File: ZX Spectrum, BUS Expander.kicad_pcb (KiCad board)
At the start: 2 copper layers, 90 x 87.4 mm, 13 parts, among them J1 Conn_02x28_Row_Letter_First, J2 Conn_02x28_Row_Letter_First

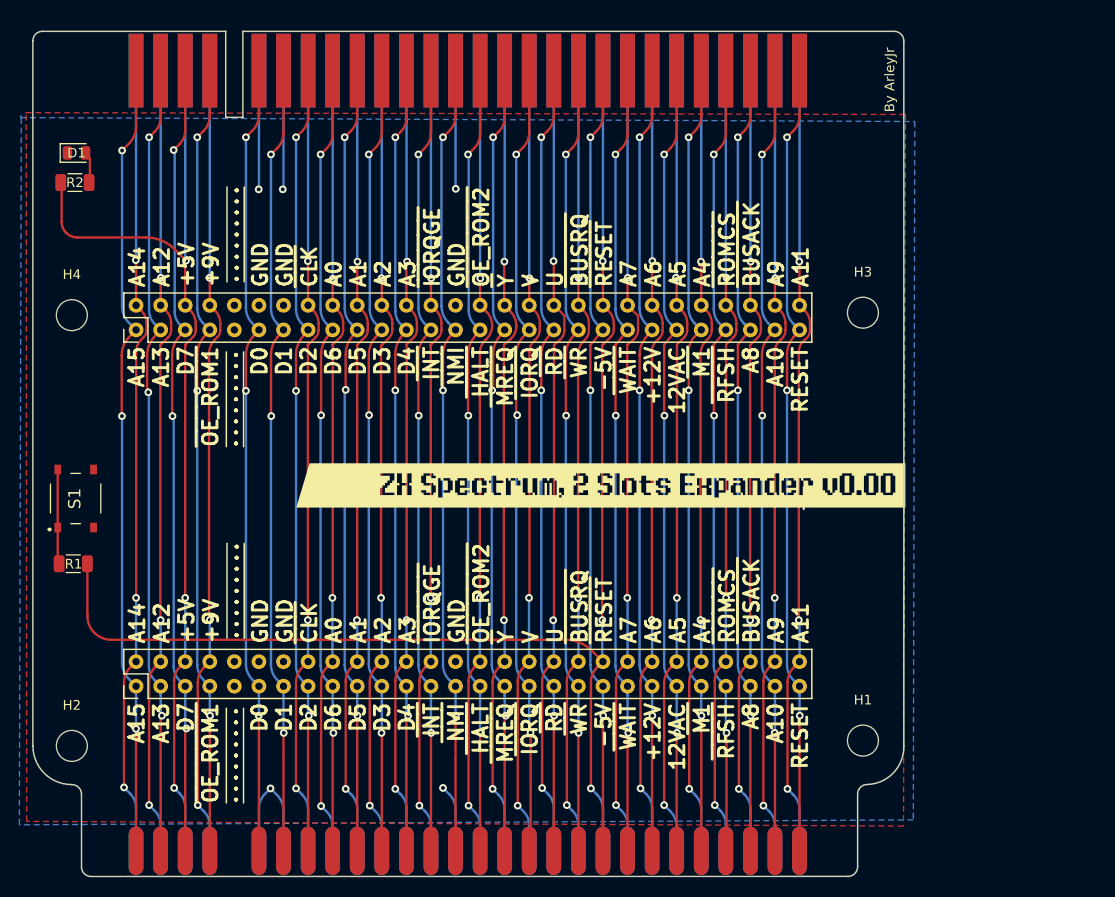
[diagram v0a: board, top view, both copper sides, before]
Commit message: Added Nemo BUS
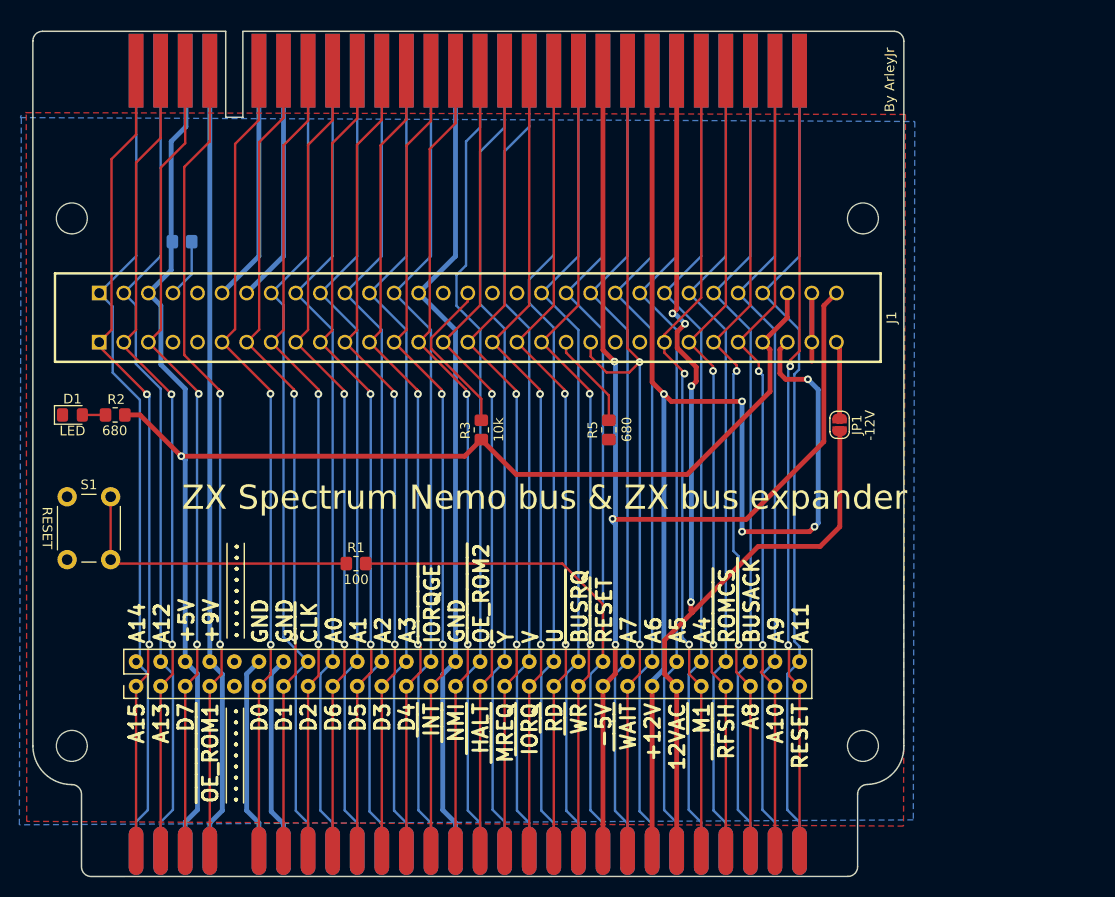
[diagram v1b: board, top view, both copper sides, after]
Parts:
- removed kibuzzard-65E37D50: G***, kibuzzard-65E37D50
- added JP1: -12V, Jumper:SolderJumper-2_P1.3mm_Open_RoundedPad1.0x1.5mm, F.Cu at (178.2, 92.4)
- added R3: 10k, Resistor_SMD:R_0805_2012Metric_Pad1.20x1.40mm_HandSolder, F.Cu at (141.2, 92.9)
- added R4: 10k, Resistor_SMD:R_0805_2012Metric_Pad1.20x1.40mm_HandSolder, B.Cu at (110.2, 73.4)
- added R5: 680, Resistor_SMD:R_0805_2012Metric_Pad1.20x1.40mm_HandSolder, F.Cu at (154.4, 92.9)
- D1: footprint LED_SMD:LED_0805_2012Metric -> LED_SMD:LED_0805_2012Metric_Pad1.15x1.40mm_HandSolder
- J1: value Conn_02x28_Row_Letter_First -> SL-62; footprint My Footprint Library, Sinclair:ZX Bus Socket -> zxbus:NemoBus-SL62-inverted
- R1: value 100R -> 100; footprint Resistor_SMD:R_1206_3216Metric -> Resistor_SMD:R_0805_2012Metric_Pad1.20x1.40mm_HandSolder
- R2: value 330R -> 680; footprint Resistor_SMD:R_1206_3216Metric -> Resistor_SMD:R_0805_2012Metric_Pad1.20x1.40mm_HandSolder
- S1: value PTS526_SM15_SMTR2_LFS -> RESET; footprint My Footprint Library:PTS526SM15SMTR2LFS -> Button_Switch_THT:SW_PUSH_6mm
- moved R1 29.2 mm to (128.2, 106.7)
- moved D1 27.1 mm to (98.9, 91.3)
- moved R2 24.4 mm to (103.3, 91.3), turned to 180 degrees
- moved H4 10.0 mm to (98.8, 71.0)
- moved H3 9.75 mm to (180.6, 71.0)
- moved S1 3.62 mm to (102.9, 99.8), turned to -90 degrees
- moved H1 0.55 mm to (180.6, 125.5)
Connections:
- J1 pad A20: -5V -> ~{IODOS}
- J1 pad A22: +12V -> unconnected-(J1-NC-PadA22)
- J1 pad A23: 12VAC -> unconnected-(J1-NC-PadA23)
- J1 pad A28: RESET/NC -> +5V
- J1 pad A4: ~{OEM_ROM1} -> unconnected-(J1-BLK-PadA4)
- J1 pad B15: ~{OE_ROM2/VIDEO} -> ~{RDR}
- J1 pad B16: ~{Y} -> RS
- J1 pad B17: V -> unconnected-(J1-NC-PadB17)
- J1 pad B18: U -> unconnected-(J1-NC-PadB18)
- J1 pad B4: +9V -> ~{DOS}
- R1 pad 1: Net-(S1-COM_1) -> Net-(R1-Pad1)
- S1 pad 1: Net-(S1-COM_1) -> Net-(R1-Pad1)
- S1 pad 2: Net-(S1-COM_1) -> GND
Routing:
- net GND: track 57.6 -> 190.4 mm, vias 5 -> 0
- net +5V: track 100.8 -> 171.2 mm, vias 3 -> 1
- net +12V: track 82.2 -> 133.7 mm, vias 3 -> 5
- net -5V: track 82.3 -> 123.5 mm
- net Net-(R1-Pad1): track 0.00 -> 31.0 mm
- net 12VAC: track 82.4 -> 113.4 mm, vias 3 -> 4
- net ~{RESET}: track 143.1 -> 117.1 mm, vias 3 -> 0
- net RS: track 0.00 -> 16.9 mm
- net ~{IODOS}: track 0.00 -> 9.90 mm
- net Net-(S1-COM_1): track 9.79 -> 0.00 mm
- net -12V: track 0.00 -> 8.03 mm
- net ~{WAIT}: track 82.4 -> 89.4 mm, vias 3 -> 2
- net ~{DOS}: track 0.00 -> 6.11 mm
- net D4: track 82.1 -> 85.6 mm, vias 3 -> 2
- net D5: track 82.2 -> 85.4 mm, vias 3 -> 2
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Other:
- board text added: "Modified by andykarpov 2024"
- board text added: "ZX Spectrum Nemo bus & ZX bus expander"
